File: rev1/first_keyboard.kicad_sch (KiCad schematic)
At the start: 83 parts, among them SW1 SW_Push, SW10 SW_Push, SW11 SW_Push, SW12 SW_Push, SW13 SW_Push, SW14 SW_Push, SW15 SW_Push, SW16 SW_Push, SW17 SW_Push, SW18 SW_Push, SW19 SW_Push, SW2 SW_Push, SW20 SW_Push, SW21 SW_Push, SW22 SW_Push, SW23 SW_Push, SW24 SW_Push, SW25 SW_Push, SW26 SW_Push, SW27 SW_Push, SW28 SW_Push, SW29 SW_Push, SW3 SW_Push, SW30 SW_Push, SW31 SW_Push, SW32 SW_Push, SW33 SW_Push, SW34 SW_Push, SW35 SW_Push, SW36 SW_Push, SW37 SW_Push, SW38 SW_Push, SW39 SW_Push, SW4 SW_Push, SW40 SW_Push, SW41 SW_Push, SW5 SW_Push, SW6 SW_Push, SW7 SW_Push, SW8 SW_Push, SW9 SW_Push, U1 Pico

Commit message: feat: スイッチとダイオードは置いた
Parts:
- added D42, D43, D44, D45, D46, D47, D48, D49, D50, D51, D52, D53, D54, D55, D56, D57, D58, D59, D60: D, symbol Device:D
- added SW42, SW43, SW44, SW45, SW46, SW47, SW48, SW49, SW50, SW51, SW52, SW53, SW54, SW55, SW56, SW57, SW58, SW59, SW60: SW_Push, symbol Switch:SW_Push
- D1, D10, D11, D12, D13, D14, D15, D16, D17, D18, D19, D2, D20, D21, D22, D23, D24, D25, D26, D27, D28, D29, D3, D30, D31, D32, D33, D34, D35, D36, D37, D38, D39, D4, D40, D41, D5, D6, D7, D8, D9: footprint kbd_Parts:Diode_TH_SMD -> (none)
- SW1, SW10, SW11, SW12, SW13, SW14, SW15, SW16, SW17, SW18, SW19, SW2, SW20, SW21, SW22, SW23, SW24, SW25, SW26, SW27, SW28, SW29, SW3, SW30, SW31, SW32, SW33, SW34, SW35, SW36, SW37, SW38, SW39, SW4, SW40, SW5, SW6, SW7, SW8, SW9: footprint kbd_SW:CherryMX_Hotswap_1u -> (none)
- SW41: footprint kbd_SW:CherryMX_Hotswap_2u -> (none)
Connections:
- net Col0: now also SW17.1, SW33.1, U1.19 (GPIO14), U1.20 (GPIO15), U1.21 (GPIO16), U1.22 (GPIO17), SW48.1, SW58.1; no longer SW2.1, SW3.1
- net Col1: now also SW18.1, SW2.1, SW34.1, SW49.1, SW59.1; no longer SW4.1, SW5.1, SW6.1
- net Col10: now also SW11.1, SW27.1, SW43.1; no longer SW37.1, SW38.1, SW39.1
- net Col11: now also SW12.1, SW28.1, SW44.1; no longer SW40.1, SW41.1
- net Col2: now also SW19.1, SW3.1, SW35.1, SW50.1, SW60.1; no longer SW7.1, SW8.1, SW9.1
- net Col3: now also SW20.1, SW36.1, SW4.1, SW51.1; no longer SW10.1, SW11.1, SW12.1, SW13.1
- net Col4: now also SW21.1, SW37.1, SW5.1, SW52.1; no longer SW14.1, SW15.1, SW16.1, SW17.1
- net Col5: now also SW22.1, SW38.1, SW6.1, SW53.1; no longer SW18.1, SW19.1, SW20.1, SW21.1
- net Col6: now also SW39.1, SW7.1, SW54.1; no longer SW22.1, SW24.1, SW25.1
- net Col7: now also SW24.1, SW40.1, SW8.1, SW55.1; no longer SW26.1, SW27.1, SW28.1, SW29.1
- net Col8: now also SW25.1, SW41.1, SW9.1, SW56.1; no longer SW30.1, SW31.1, SW32.1, SW33.1
- net Col9: now also SW10.1, SW26.1, SW42.1, SW57.1; no longer SW34.1, SW35.1, SW36.1
- removed net Row0: D1.1 (K), D10.1 (K), D14.1 (K), D18.1 (K), D22.1 (K), D26.1 (K), D30.1 (K), D34.1 (K), D37.1 (K), D4.1 (K), D40.1 (K), D7.1 (K), U1.19 (GPIO14)
- removed net Row1: D11.1 (K), D15.1 (K), D19.1 (K), D2.1 (K), D23.1 (K), D27.1 (K), D31.1 (K), D35.1 (K), D38.1 (K), D41.1 (K), D5.1 (K), D8.1 (K), U1.20 (GPIO15)
- removed net Row2: D12.1 (K), D16.1 (K), D20.1 (K), D24.1 (K), D28.1 (K), D3.1 (K), D32.1 (K), D36.1 (K), D39.1 (K), D6.1 (K), D9.1 (K), U1.21 (GPIO16)
- net Row3: no longer names the net of D17.1 (K), D21.1 (K), D25.1 (K), D29.1 (K)
- net Row3: now also D18.1 (K), D19.1 (K), D20.1 (K), D22.1 (K), D23.1 (K), D24.1 (K), D26.1 (K), D27.1 (K), D28.1 (K), D30.1 (K), D31.1 (K), D32.1 (K); no longer D13.1 (K), D33.1 (K), U1.22 (GPIO17)
- new net: D33.1 (K), D34.1 (K), D35.1 (K), D36.1 (K), D37.1 (K), D38.1 (K), D39.1 (K), D40.1 (K), D41.1 (K), D42.1 (K), D43.1 (K), D44.1 (K), D45.1 (K), D46.1 (K), D47.1 (K)
- new net: D42.2 (A), SW42.2
- new net: D58.1 (K), D59.1 (K), D60.1 (K)
- new net: D60.2 (A), SW60.2
- new net: D51.2 (A), SW51.2
- new net: D44.2 (A), SW44.2
- new net: D1.1 (K), D10.1 (K), D11.1 (K), D12.1 (K), D13.1 (K), D14.1 (K), D15.1 (K), D16.1 (K), D2.1 (K), D3.1 (K), D4.1 (K), D5.1 (K), D6.1 (K), D7.1 (K), D8.1 (K), D9.1 (K)
- new net: D46.2 (A), SW46.2
- new net: D43.2 (A), SW43.2
- new net: D49.2 (A), SW49.2
- new net: D58.2 (A), SW58.2
- new net: D59.2 (A), SW59.2
- new net: D55.2 (A), SW55.2
- new net: D48.1 (K), D49.1 (K), D50.1 (K), D51.1 (K), D52.1 (K), D53.1 (K), D54.1 (K), D55.1 (K), D56.1 (K), D57.1 (K)
- new net: D53.2 (A), SW53.2
- new net: D45.2 (A), SW45.2
- new net: D48.2 (A), SW48.2
- new net: D50.2 (A), SW50.2
- new net: D57.2 (A), SW57.2
- new net: D47.2 (A), SW47.2
- new net: D52.2 (A), SW52.2
- new net: D54.2 (A), SW54.2
- new net: D56.2 (A), SW56.2
- new net Col12: SW13.1, SW29.1, SW45.1
- new net Col13: SW14.1, SW30.1, SW46.1
- new net Col14: SW15.1, SW31.1, SW47.1
- new net Col15: SW16.1, SW32.1

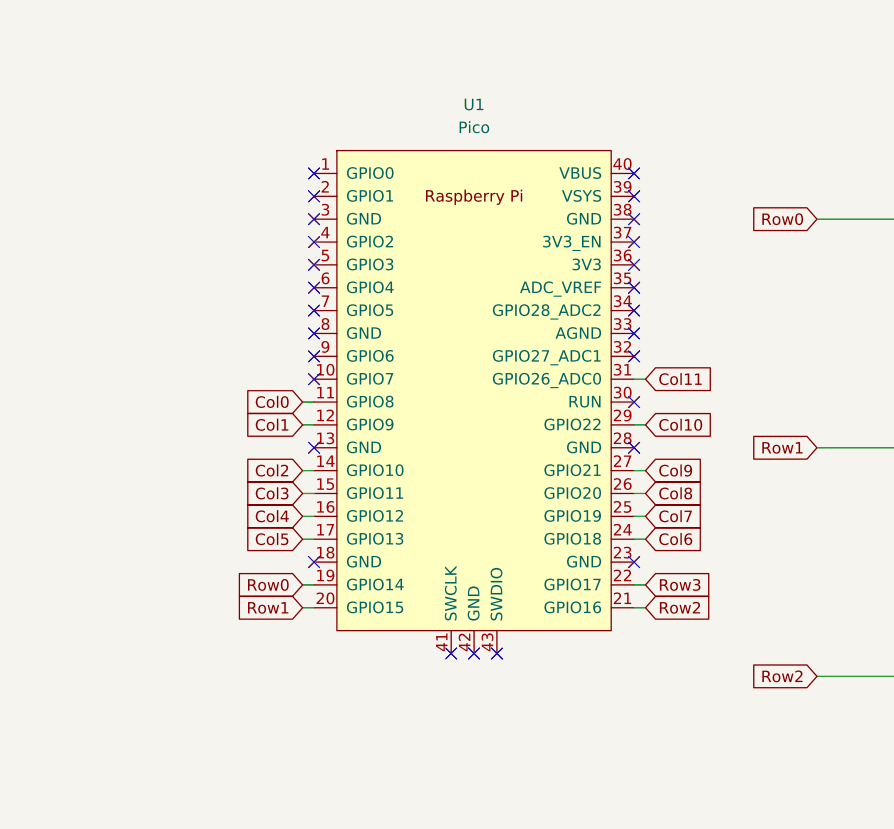
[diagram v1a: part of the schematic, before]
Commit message: feat: 回路図引いた
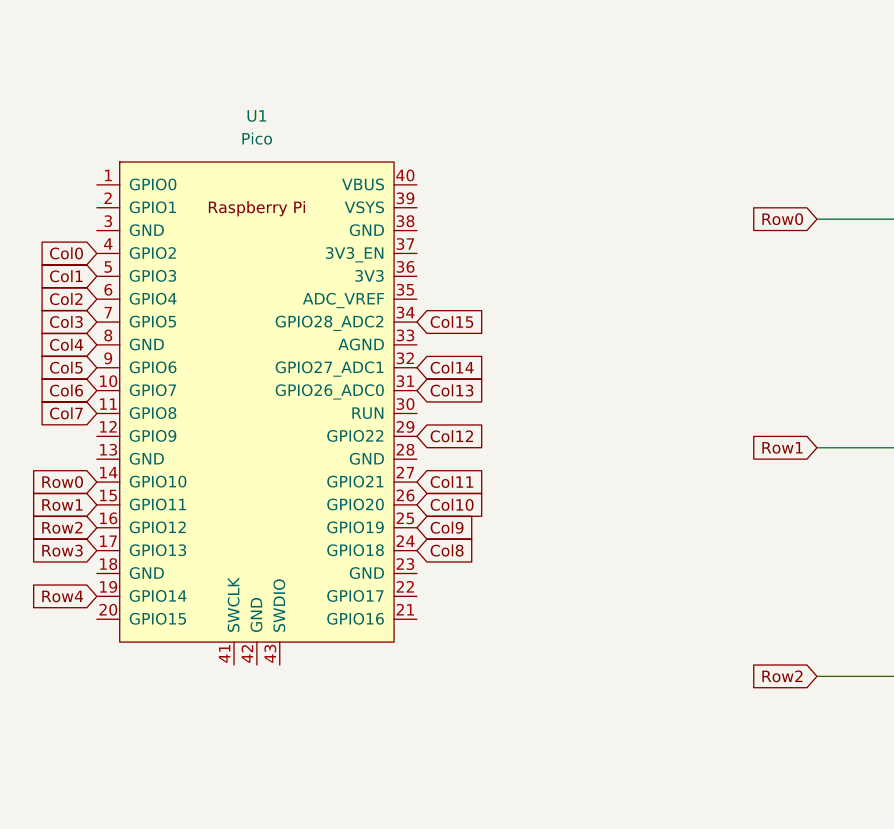
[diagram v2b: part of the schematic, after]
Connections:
- net Col0: now also U1.14 (GPIO10), U1.15 (GPIO11), U1.16 (GPIO12), U1.17 (GPIO13), U1.4 (GPIO2); no longer U1.11 (GPIO8), U1.20 (GPIO15), U1.21 (GPIO16), U1.22 (GPIO17)
- net Col1: now also U1.5 (GPIO3); no longer U1.12 (GPIO9)
- net Col10: now also U1.26 (GPIO20); no longer U1.29 (GPIO22)
- net Col11: now also U1.27 (GPIO21); no longer U1.31 (GPIO26_ADC0)
- net Col12: now also U1.29 (GPIO22)
- net Col13: now also U1.31 (GPIO26_ADC0)
- net Col14: now also U1.32 (GPIO27_ADC1)
- net Col15: now also U1.34 (GPIO28_ADC2)
- net Col2: now also U1.6 (GPIO4); no longer U1.14 (GPIO10)
- net Col3: now also U1.7 (GPIO5); no longer U1.15 (GPIO11)
- net Col4: now also U1.8 (GND); no longer U1.16 (GPIO12)
- net Col5: now also U1.9 (GPIO6); no longer U1.17 (GPIO13)
- net Col6: now also U1.10 (GPIO7); no longer U1.24 (GPIO18)
- net Col7: now also U1.11 (GPIO8); no longer U1.25 (GPIO19)
- net Col8: now also U1.24 (GPIO18); no longer U1.26 (GPIO20)
- net Col9: now also U1.25 (GPIO19); no longer U1.27 (GPIO21)
- no-connect marks 27 -> 0

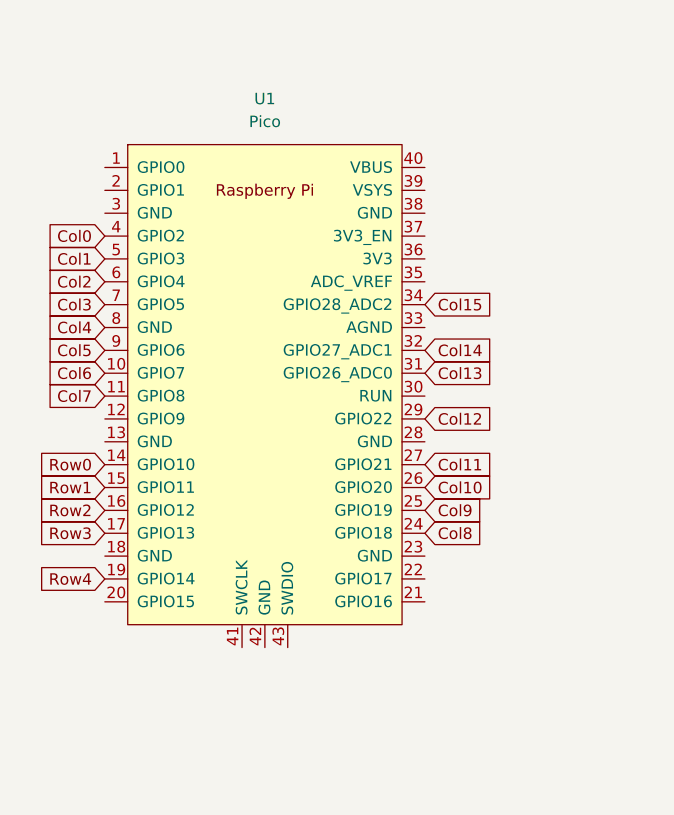
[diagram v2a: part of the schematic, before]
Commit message: feat: ラベル付け直しとフットプリント指定
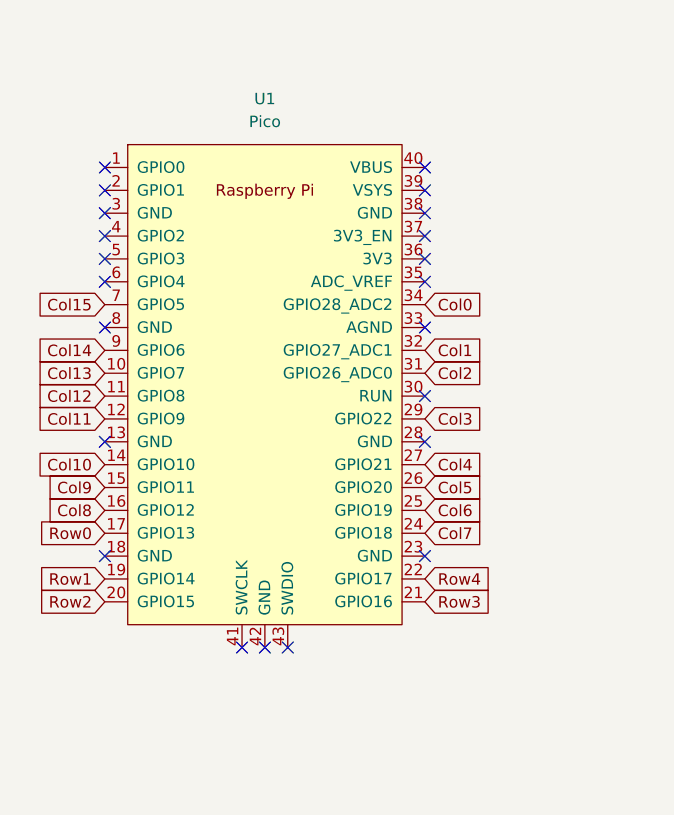
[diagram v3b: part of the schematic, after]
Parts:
- D1, D10, D11, D12, D13, D14, D15, D16, D17, D18, D19, D2, D20, D21, D22, D23, D24, D25, D26, D27, D28, D29, D3, D30, D31, D32, D33, D34, D35, D36, D37, D38, D39, D4, D40, D41, D42, D43, D44, D45, D46, D47, D48, D49, D5, D50, D51, D52, D53, D54, D55, D56, D57, D58, D59, D6, D60, D7, D8, D9: footprint (none) -> kbd_Parts:Diode_TH_SMD
- SW1, SW10, SW11, SW12, SW13, SW14, SW15, SW16, SW17, SW18, SW19, SW2, SW20, SW21, SW22, SW23, SW24, SW25, SW26, SW27, SW28, SW29, SW3, SW30, SW31, SW33, SW34, SW35, SW36, SW37, SW38, SW39, SW4, SW40, SW41, SW42, SW43, SW44, SW45, SW46, SW47, SW48, SW49, SW5, SW50, SW51, SW52, SW53, SW54, SW55, SW56, SW57, SW59, SW6, SW60, SW7, SW8, SW9: footprint (none) -> kbd_SW:CherryMX_Hotswap_1u
- SW32, SW58: footprint (none) -> kbd_SW:CherryMX_Hotswap_2u
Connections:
- net Col0: now also U1.20 (GPIO15), U1.21 (GPIO16), U1.22 (GPIO17), U1.34 (GPIO28_ADC2); no longer U1.14 (GPIO10), U1.15 (GPIO11), U1.16 (GPIO12), U1.4 (GPIO2)
- net Col1: now also U1.32 (GPIO27_ADC1); no longer U1.5 (GPIO3)
- net Col10: now also U1.14 (GPIO10); no longer U1.26 (GPIO20)
- net Col11: now also U1.12 (GPIO9); no longer U1.27 (GPIO21)
- net Col12: now also U1.11 (GPIO8); no longer U1.29 (GPIO22)
- net Col13: now also U1.10 (GPIO7); no longer U1.31 (GPIO26_ADC0)
- net Col14: now also U1.9 (GPIO6); no longer U1.32 (GPIO27_ADC1)
- net Col15: now also U1.7 (GPIO5); no longer U1.34 (GPIO28_ADC2)
- net Col2: now also U1.31 (GPIO26_ADC0); no longer U1.6 (GPIO4)
- net Col3: now also U1.29 (GPIO22); no longer U1.7 (GPIO5)
- net Col4: now also U1.27 (GPIO21); no longer U1.8 (GND)
- net Col5: now also U1.26 (GPIO20); no longer U1.9 (GPIO6)
- net Col6: now also U1.25 (GPIO19); no longer U1.10 (GPIO7)
- net Col7: now also U1.24 (GPIO18); no longer U1.11 (GPIO8)
- net Col8: now also U1.16 (GPIO12); no longer U1.24 (GPIO18)
- net Col9: now also U1.15 (GPIO11); no longer U1.25 (GPIO19)
- no-connect marks 0 -> 22
